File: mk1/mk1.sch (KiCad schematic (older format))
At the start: 121 parts, among them U1 STM32F070CBTx

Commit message: using ML switch built i jumper bar
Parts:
- removed D? (x59): 1N4148, symbol Device:D_Small_ALT
- removed SW? (x60): SW_Push, symbol Switch:SW_Push
- added D10, D11, D12, D13, D14, D15, D16, D17, D18, D19, D2, D20, D21, D22, D23, D24, D25, D26, D27, D28, D29, D3, D30, D31, D32, D33, D34, D35, D36, D37, D38, D39, D4, D40, D41, D42, D43, D44, D45, D46, D47, D48, D49, D5, D50, D51, D52, D53, D54, D55, D56, D57, D58, D59, D6, D60, D7, D8, D9: 1N4148, Diode_SMD:D_SOD-123, symbol Device:D_Small_ALT
- added U10, U11, U12, U13, U14, U15, U16, U17, U18, U19, U2, U20, U21, U22, U23, U24, U25, U26, U27, U28, U29, U3, U30, U31, U32, U33, U34, U35, U36, U37, U38, U39, U4, U40, U41, U42, U43, U44, U45, U46, U47, U48, U49, U5, U50, U51, U52, U53, U54, U55, U56, U57, U58, U59, U6, U60, U61, U7, U8, U9: CHERRY_ML, Switches:CHERRY_ML, symbol keyswitch:CHERRY_ML
- D1: renamed from D?; footprint (none) -> Diode_SMD:D_SOD-123
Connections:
- net COL0: now also D1.1 (K), D2.1 (K), D3.1 (K), D4.1 (K), D5.1 (K)
- net COL1: now also D10.1 (K), D6.1 (K), D7.1 (K), D8.1 (K), D9.1 (K)
- net COL10: now also D51.1 (K), D52.1 (K), D53.1 (K), D54.1 (K), D55.1 (K)
- net COL11: now also D56.1 (K), D57.1 (K), D58.1 (K), D59.1 (K), D60.1 (K)
- net COL2: now also D11.1 (K), D12.1 (K), D13.1 (K), D14.1 (K), D15.1 (K)
- net COL3: now also D16.1 (K), D17.1 (K), D18.1 (K), D19.1 (K), D20.1 (K)
- net COL4: now also D21.1 (K), D22.1 (K), D23.1 (K), D24.1 (K), D25.1 (K)
- net COL5: now also D26.1 (K), D27.1 (K), D28.1 (K), D29.1 (K), D30.1 (K)
- net COL6: now also D31.1 (K), D32.1 (K), D33.1 (K), D34.1 (K), D35.1 (K)
- net COL7: now also D36.1 (K), D37.1 (K), D38.1 (K), D39.1 (K), D40.1 (K)
- net COL8: now also D41.1 (K), D42.1 (K), D43.1 (K), D44.1 (K), D45.1 (K)
- net COL9: now also D46.1 (K), D47.1 (K), D48.1 (K), D49.1 (K), D50.1 (K)
- net ROW0: now also U2.1, U2.3, U3.1, U3.3, U4.1, U4.3, U5.1, U5.3, U6.1, U6.3; no longer D1.1 (K)
- net at D1.2 (A): now also U2.2
- new net: U2.4, U7.1, U7.3
- new net: D6.2 (A), U7.2
- new net: U12.1, U12.3, U7.4
- new net: D11.2 (A), U12.2
- new net: U12.4, U17.1, U17.3
- new net: D16.2 (A), U17.2
- new net: U17.4, U22.1, U22.3
- new net: D21.2 (A), U22.2
- new net: U22.4, U27.1, U27.3
- new net: D26.2 (A), U27.2
- new net: U27.4, U32.1, U32.3
- new net: D31.2 (A), U32.2
- new net: U32.4, U37.1, U37.3
- new net: D36.2 (A), U37.2
- new net: U37.4, U42.1, U42.3
- new net: D41.2 (A), U42.2
- new net: U42.4, U47.1, U47.3
- new net: D46.2 (A), U47.2
- new net: U47.4, U52.1, U52.3
- new net: D51.2 (A), U52.2
- new net: U52.4, U57.1, U57.3
- new net: D56.2 (A), U57.2
- new net: D2.2 (A), U3.2
- new net: U3.4, U8.1, U8.3
- new net: D7.2 (A), U8.2
- new net: U13.1, U13.3, U8.4
- new net: D12.2 (A), U13.2
- new net: U13.4, U18.1, U18.3
- new net: D17.2 (A), U18.2
- new net: U18.4, U23.1, U23.3
- new net: D22.2 (A), U23.2
- new net: U23.4, U28.1, U28.3
- new net: D27.2 (A), U28.2
- new net: U28.4, U33.1, U33.3
- new net: D32.2 (A), U33.2
- new net: U33.4, U38.1, U38.3
- new net: D37.2 (A), U38.2
- new net: U38.4, U43.1, U43.3
- new net: D42.2 (A), U43.2
- new net: U43.4, U48.1, U48.3
- new net: D47.2 (A), U48.2
- new net: U48.4, U53.1, U53.3
- new net: D52.2 (A), U53.2
- new net: U53.4, U58.1, U58.3
- new net: D57.2 (A), U58.2
- new net: D3.2 (A), U4.2
- new net: U4.4, U9.1, U9.3
- new net: D8.2 (A), U9.2
- new net: U14.1, U14.3, U9.4
- new net: D13.2 (A), U14.2
- new net: U14.4, U19.1, U19.3
- new net: D18.2 (A), U19.2
- new net: U19.4, U24.1, U24.3
- new net: D23.2 (A), U24.2
- new net: U24.4, U29.1, U29.3
- new net: D28.2 (A), U29.2
- new net: U29.4, U34.1, U34.3
- new net: D33.2 (A), U34.2
- new net: U34.4, U39.1, U39.3
- new net: D38.2 (A), U39.2
- new net: U39.4, U44.1, U44.3
- new net: D43.2 (A), U44.2
- new net: U44.4, U49.1, U49.3
- new net: D48.2 (A), U49.2
- new net: U49.4, U54.1, U54.3
- new net: D53.2 (A), U54.2
- new net: U54.4, U59.1, U59.3
- new net: D58.2 (A), U59.2
- new net: D4.2 (A), U5.2
- new net: U10.1, U10.3, U5.4
- new net: D9.2 (A), U10.2
- new net: U10.4, U15.1, U15.3
- new net: D14.2 (A), U15.2
- new net: U15.4, U20.1, U20.3
- new net: D19.2 (A), U20.2
- new net: U20.4, U25.1, U25.3
- new net: D24.2 (A), U25.2
- new net: U25.4, U30.1, U30.3
- new net: D29.2 (A), U30.2
- new net: U30.4, U35.1, U35.3
- new net: D34.2 (A), U35.2
- new net: U35.4, U40.1, U40.3
- new net: D39.2 (A), U40.2
- new net: U40.4, U45.1, U45.3
- new net: D44.2 (A), U45.2
- new net: U45.4, U50.1, U50.3
- new net: D49.2 (A), U50.2
- new net: U50.4, U55.1, U55.3
- new net: D54.2 (A), U55.2
- new net: U55.4, U60.1, U60.3
- new net: D59.2 (A), U60.2
- new net: D5.2 (A), U6.2
- new net: U11.1, U11.3, U6.4
- new net: D10.2 (A), U11.2
- new net: U11.4, U16.1, U16.3
- new net: D15.2 (A), U16.2
- new net: U16.4, U21.1, U21.3
- new net: D20.2 (A), U21.2
- new net: U21.4, U26.1, U26.3
- new net: D25.2 (A), U26.2
- new net: U26.4, U31.1, U31.3
- new net: D30.2 (A), U31.2
- new net: U31.4, U36.1, U36.3
- new net: D35.2 (A), U36.2
- new net: U36.4, U41.1, U41.3
- new net: D40.2 (A), U41.2
- new net: U41.4, U46.1, U46.3
- new net: D45.2 (A), U46.2
- new net: U46.4, U51.1, U51.3
- new net: D50.2 (A), U51.2
- new net: U51.4, U56.1, U56.3
- new net: D55.2 (A), U56.2
- new net: U56.4, U61.1, U61.3
- new net: D60.2 (A), U61.2
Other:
- moved on the sheet: D1

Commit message: more keys
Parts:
- added C1, C2: 12p, Capacitor_SMD:C_0603_1608Metric, symbol Device:C_Small
- added C3, C4, C5, C6, C7: 100n, Capacitor_SMD:C_0603_1608Metric, symbol Device:C_Small
- added D61, D62, D63, D64, D65, D66, D67, D68, D69, D70, D71, D72, D73, D74, D75, D76, D77, D78, D79, D80, D81, D82, D83, D84, D89, D90, D91, D92: 1N4148, Diode_SMD:D_SOD-123, symbol Device:D_Small_ALT
- added D85, D86, D87, D88: LED_Small_ALT, LED_THT:LED_D3.0mm, symbol Device:LED_Small_ALT
- added J1: JTAG, Connector_PinHeader_1.27mm:PinHeader_2x05_P1.27mm_Vertical, symbol Connector_Generic:Conn_02x05_Odd_Even
- added J2: USB_B_Micro, Connector_USB:USB_Micro-B_Molex-105017-0001, symbol connector:USB_B_Micro
- added J3: Conn_01x04, Connector_PinHeader_2.54mm:PinHeader_1x04_P2.54mm_Vertical, symbol Connector_Generic:Conn_01x04
- added R1, R2, R3, R4: 330, Resistor_SMD:R_0603_1608Metric, symbol Device:R_Small
- added R5: 10k, Resistor_SMD:R_0603_1608Metric, symbol Device:R_Small
- added SW1: BOOT, Button_Switch_SMD:SW_SPST_B3U-1000P, symbol Switch:SW_Push
- added SW2: RESET, Button_Switch_SMD:SW_SPST_B3U-1000P, symbol Switch:SW_Push
- added U62, U63, U64, U65, U66, U67, U68, U69, U70, U71, U72, U73, U74, U75, U76, U77, U78, U79, U80, U81, U82, U83, U84, U85, U86, U87, U88, U89: CHERRY_ML, Switches:CHERRY_ML, symbol keyswitch:CHERRY_ML
- added X1: 8 MHz, Crystal:Crystal_SMD_5032-2Pin_5.0x3.2mm, symbol Device:Crystal_Small
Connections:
- net labels added: +3V3, +5V, DBG_RX, DBG_TX, GND, LED0, LED1, LED2, LED3, NRST, ROW1, ROW2, ROW3, ROW4, ROW5, ROW6, ROW7, RX, SWCLK, SWDIO, TX, USBD+, USBD-
- wire segments 240 -> 446
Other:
- note added: "a few random LEDs"
- moved on the sheet: D1, D10, D11, D12, D13, D14, D15, D16, D17, D18, D19, D2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

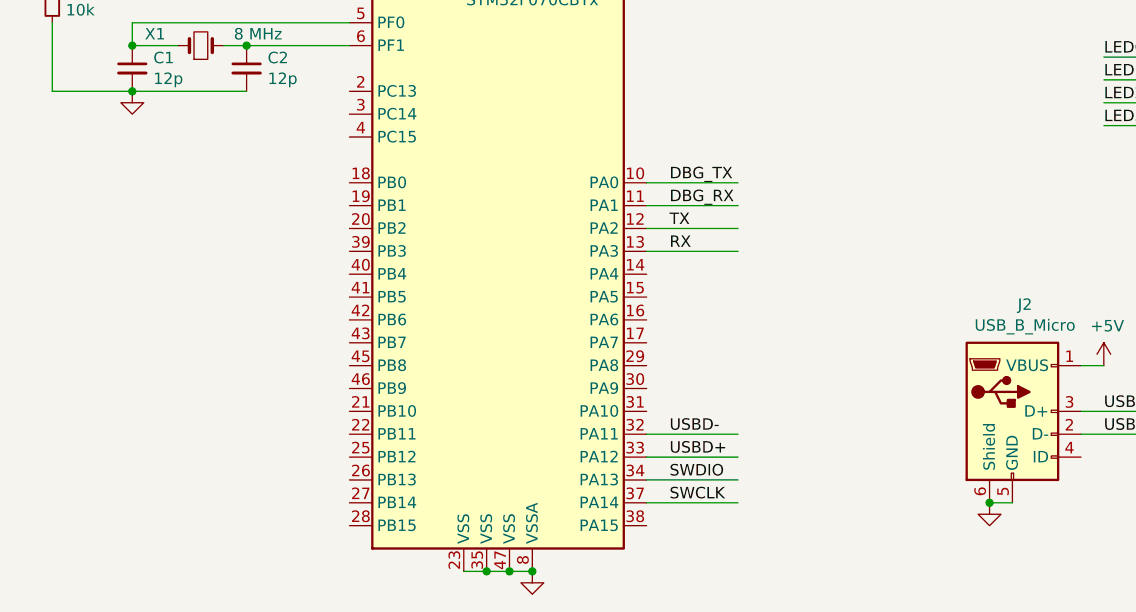
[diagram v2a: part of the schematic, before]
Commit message: add mcu pin peripheral labels
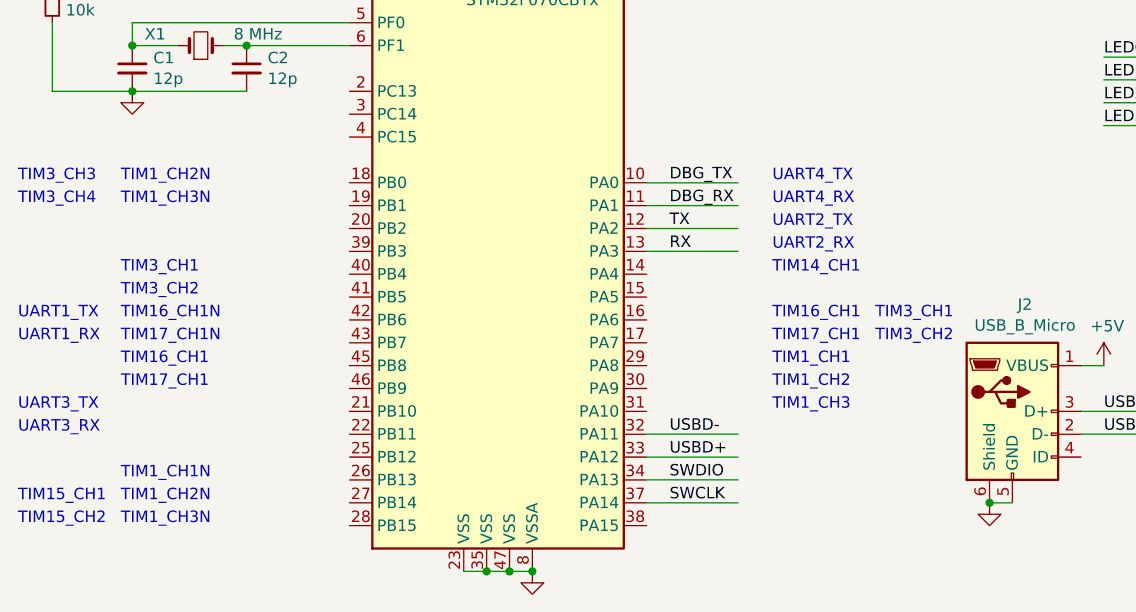
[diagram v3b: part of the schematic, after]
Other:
- note added: "TIM14_CH1"
- note added: "TIM15_CH1"
- note added: "TIM15_CH2"
- note added: "TIM16_CH1"
- note added: "TIM16_CH1N"
- note added: "TIM17_CH1"
- note added: "TIM17_CH1N"
- note added: "TIM1_CH1"
- note added: "TIM1_CH1N"
- note added: "TIM1_CH2"
- note added: "TIM1_CH2N"
- note added: "TIM1_CH3"
- note added: "TIM1_CH3N"
- note added: "TIM3_CH1"
- note added: "TIM3_CH2"
- note added: "TIM3_CH3"
- note added: "TIM3_CH4"
- note added: "UART1_RX"
- note added: "UART1_TX"
- note added: "UART2_RX"
- note added: "UART2_TX"
- note added: "UART3_RX"
- note added: "UART3_TX"
- note added: "UART4_RX"
- note added: "UART4_TX"
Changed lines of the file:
@@
 Wire Wire Line
 	6650 7450 6250 7450
+Text Notes 3850 6400 0    50   ~ 0
+TIM14_CH1
+Text Notes 3850 6600 0    50   ~ 0
+TIM16_CH1
+Text Notes 3850 6700 0    50   ~ 0
+TIM17_CH1
+Text Notes 4300 6600 0    50   ~ 0
+TIM3_CH1
+Text Notes 4300 6700 0    50   ~ 0
+TIM3_CH2
+Text Notes 3850 6800 0    50   ~ 0
+TIM1_CH1
+Text Notes 3850 6900 0    50   ~ 0
+TIM1_CH2
+Text Notes 3850 7000 0    50   ~ 0
+TIM1_CH3
+Text Notes 1000 6000 0    50   ~ 0
+TIM1_CH2N
+Text Notes 1000 6100 0    50   ~ 0
+TIM1_CH3N
+Text Notes 550  6000 0    50   ~ 0
+TIM3_CH3
+Text Notes 550  6100 0    50   ~ 0
+TIM3_CH4
+Text Notes 1000 6400 0    50   ~ 0
+TIM3_CH1
+Text Notes 1000 6500 0    50   ~ 0
+TIM3_CH2
+Text Notes 1000 6600 0    50   ~ 0
+TIM16_CH1N
+Text Notes 1000 6700 0    50   ~ 0
+TIM17_CH1N
+Text Notes 1000 6800 0    50   ~ 0
+TIM16_CH1
+Text Notes 1000 6900 0    50   ~ 0
+TIM17_CH1
+Text Notes 550  7000 0    50   ~ 0
+UART3_TX
+Text Notes 550  7100 0    50   ~ 0
+UART3_RX
+Text Notes 1000 7300 0    50   ~ 0
+TIM1_CH1N
+Text Notes 1000 7400 0    50   ~ 0
+TIM1_CH2N
+Text Notes 1000 7500 0    50   ~ 0
+TIM1_CH3N
+Text Notes 550  7400 0    50   ~ 0
+TIM15_CH1
+Text Notes 550  7500 0    50   ~ 0
+TIM15_CH2
+Text Notes 550  6600 0    50   ~ 0
+UART1_TX
+Text Notes 550  6700 0    50   ~ 0
+UART1_RX
+Text Notes 3850 6200 0    50   ~ 0
+UART2_TX
+Text Notes 3850 6300 0    50   ~ 0
+UART2_RX
+Text Notes 3850 6000 0    50   ~ 0
+UART4_TX
+Text Notes 3850 6100 0    50   ~ 0
+UART4_RX
 $EndSCHEMATC

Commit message: route a few columns
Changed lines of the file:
@@
 Text Notes 3850 6100 0    50   ~ 0
 UART4_RX
+Text Label 1750 4550 0    50   ~ 0
+NRST
 $EndSCHEMATC
